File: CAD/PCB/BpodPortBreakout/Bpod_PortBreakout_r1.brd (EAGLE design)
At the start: 49.9 x 49.1 mm, 9 parts

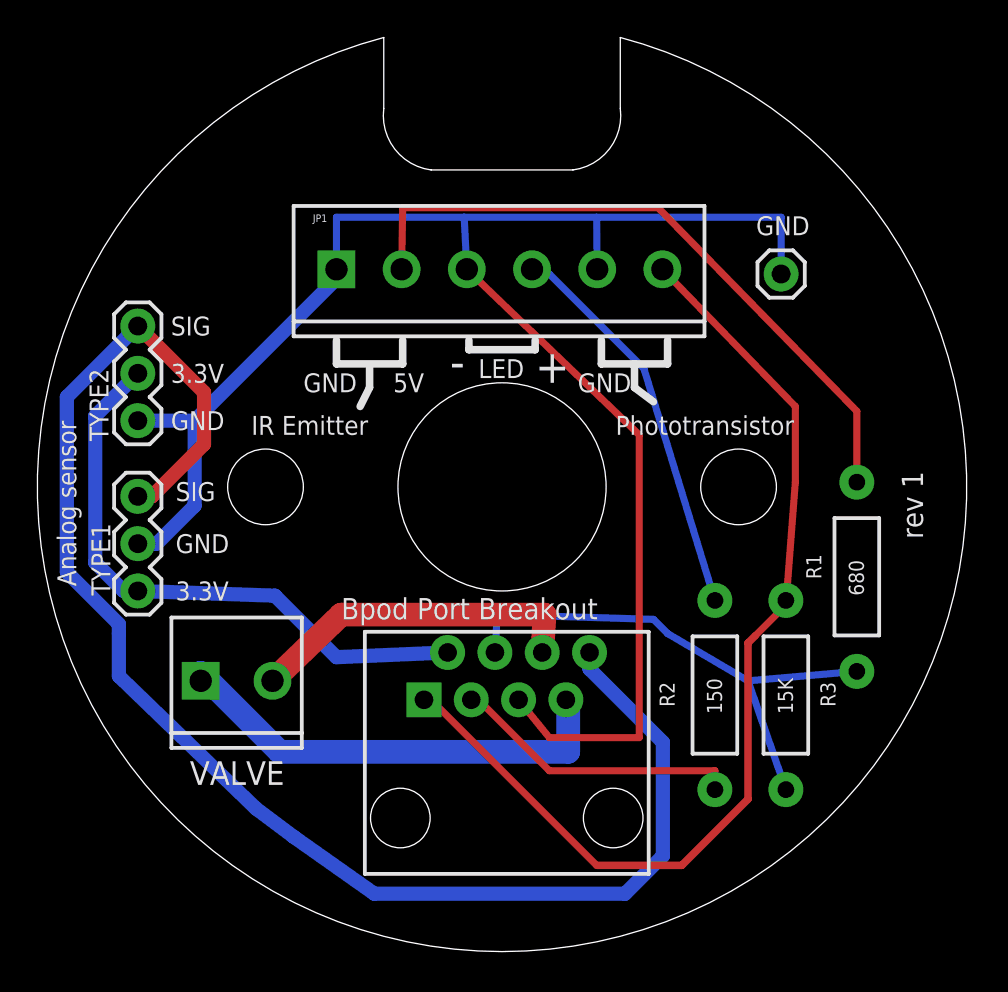
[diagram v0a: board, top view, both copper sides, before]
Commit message: Major update: -Integrates with PsychToolbox (if installed) for low latency serial and possible future use as a sound server -Adds sound support with Teensy Audio board, added as a hardware serial device -Updated to work on Ubuntu 14 with MATLAB r2011a or newer (must create a serial port alias: /dev/TTYACM0 --> /dev/TTYS101) -Added hardware serial override to GUI -Many other bug-fixes
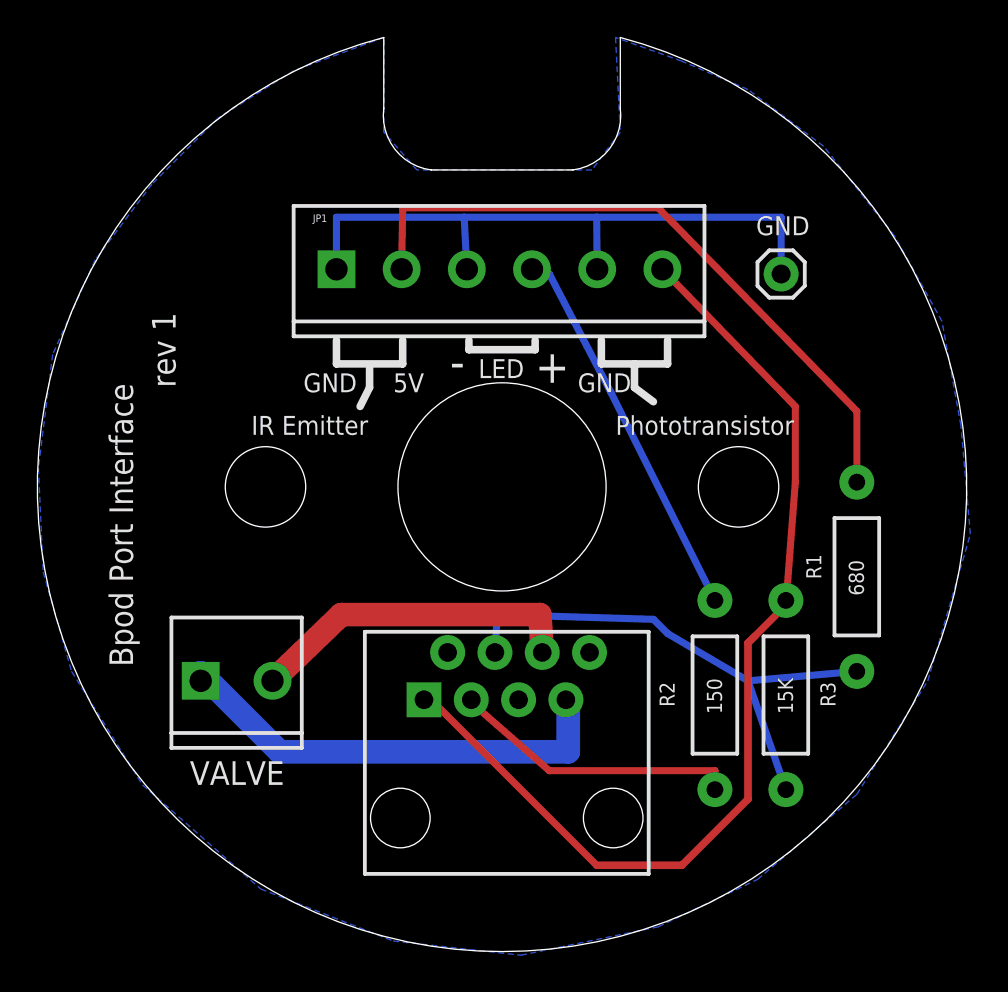
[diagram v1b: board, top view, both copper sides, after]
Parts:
- removed TYPE1, TYPE2: (no value), SparkFun:1X03
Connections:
- removed net N$11: TYPE1.1, TYPE2.3, U$1.8
- removed net N$9: TYPE1.3, TYPE2.2, U$1.2
- net N$4: no longer TYPE1.2, TYPE2.1
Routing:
- net N$11: track 81.0 -> 0.00 mm
- net N$4: track 94.6 -> 35.8 mm
- net N$9: track 32.0 -> 0.00 mm
- net N$7: track 21.2 -> 20.6 mm
- added copper zone on layer 16, net N$4
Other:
- outline, holes or cut-outs redrawn
- board text added: "Bpod Port Interface"
- board text removed: "3.3V"
- board text removed: "Analog sensor"
- board text removed: "Bpod Port Breakout"
- board text removed: "SIG"
